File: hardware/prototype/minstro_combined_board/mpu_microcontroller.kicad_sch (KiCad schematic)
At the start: 48 parts, among them J401 BOOT, J402 I2C, J403 USB_C_Receptacle_USB2.0_16P, J404 SDMMC 4b, J405 Conn_Coaxial, SW401 RST, U401 ESP32-S3, U402 W25Q128JVS, Y401 40 MHz

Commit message: Layout WIP
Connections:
- net STATUS_LED: now also U401.51 (GPIO45); no longer U401.10 (GPIO5)
- net at J405.1 (In): now also JP401.3 (B); no longer JP401.1 (A)
- net at AE401.1 (A): now also JP401.1 (A); no longer JP401.3 (B)
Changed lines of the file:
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@@
 	)
 	(label "STATUS_LED"
-		(at 57.15 85.09 180)
+		(at 114.3 124.46 0)
 		(effects
 			(font
 				(size 1.27 1.27)
 			)
-			(justify right bottom)
+			(justify left bottom)
 		)
 	)
@@
 		)
 	)
+	(netclass_flag ""
+		(length 2.54)
+		(shape round)
+		(at 57.15 170.18 90)
+		(fields_autoplaced yes)
+		(effects
+			(font
+				(size 1.27 1.27)
+			)
+			(justify left bottom)
+		)
+		(property "Netclass" "50ohm"
+			(at 54.61 169.4815 90)
+			(effects
+				(font
+					(size 1.27 1.27)
+				)
+				(justify left)
+			)
+		)
+		(property "Component Class" ""
+			(at -10.16 3.81 0)
+			(effects
+				(font
+					(size 1.27 1.27)
+					(italic yes)
+				)
+			)
+		)
+	)
+	(netclass_flag ""
+		(length 2.54)
+		(shape round)
+		(at 57.15 184.15 180)
+		(fields_autoplaced yes)
+		(effects
+			(font
+				(size 1.27 1.27)
+			)
+			(justify right bottom)
+		)
+		(property "Netclass" "50ohm"
+			(at 57.8485 186.69 0)
+			(effects
+				(font
+					(size 1.27 1.27)
+				)
+				(justify left)
+			)
+		)
+		(property "Component Class" ""
+			(at -10.16 17.78 0)
+			(effects
+				(font
+					(size 1.27 1.27)
+					(italic yes)
+				)
+			)
+		)
+	)
 	(symbol
 		(lib_id "Device:C_Small")
@@
 		(lib_id "Jumper:SolderJumper_3_Open")
 		(at 57.15 176.53 270)
-		(mirror x)
 		(unit 1)
 		(exclude_from_sim yes)
@@
 		)
 		(property "Value" "SolderJumper_3_Open"
-			(at 59.436 174.244 90)
+			(at 59.436 178.816 90)
 			(effects
 				(font

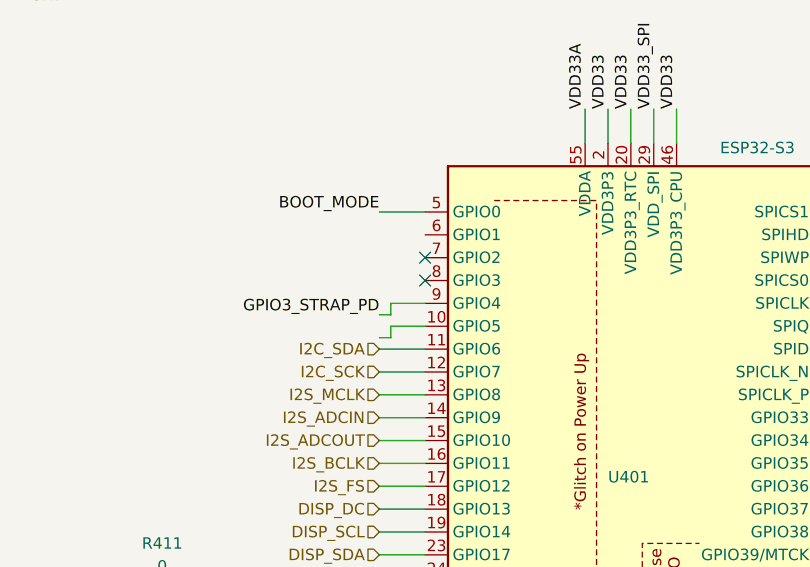
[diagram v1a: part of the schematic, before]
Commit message: Bringup WIP.  I2C enumerating.
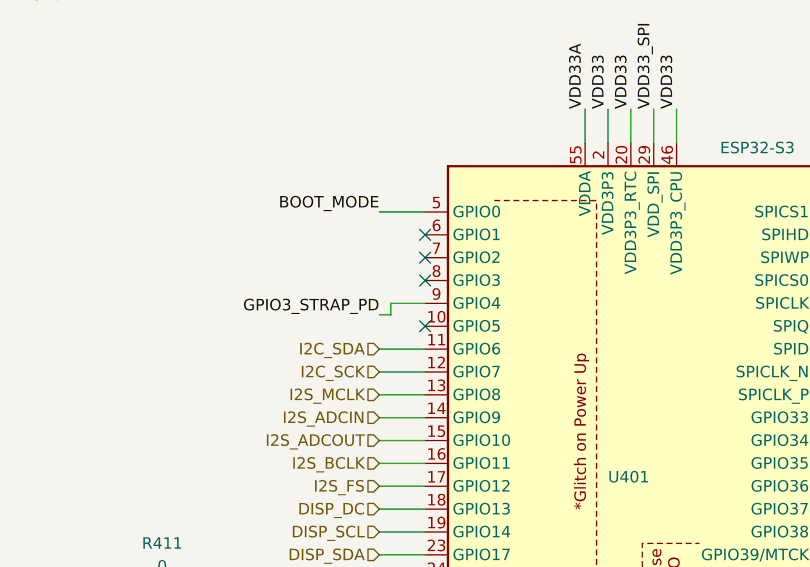
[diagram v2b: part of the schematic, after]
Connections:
- no-connect marks 10 -> 12
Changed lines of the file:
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@@
+	)
+	(no_connect
+		(at 62.23 83.82)
 	)
 	(no_connect
@@
 	)
 	(no_connect
+		(at 62.23 73.66)
+	)
+	(no_connect
 		(at 259.08 149.86)
 	)
@@
 	(wire
 		(pts
-			(xy 58.42 83.82) (xy 62.23 83.82)
-		)
-		(stroke
-			(width 0)
-			(type default)
-		)
-	)
-	(wire
-		(pts
 			(xy 57.15 101.6) (xy 62.23 101.6)
 		)
@@
 	(wire
 		(pts
-			(xy 58.42 85.09) (xy 58.42 83.82)
-		)
-		(stroke
-			(width 0)
-			(type default)
-		)
-	)
-	(wire
-		(pts
 			(xy 60.96 119.38) (xy 62.23 119.38)
 		)
@@
 		)
 		(stroke
-			(width 0)
-			(type default)
-		)
-	)
-	(wire
-		(pts
-			(xy 57.15 85.09) (xy 58.42 85.09)
-		)
-		(stroke
